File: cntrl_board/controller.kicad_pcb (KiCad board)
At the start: 2 copper layers, 223.5 x 91.7 mm, 419 parts, among them J1 PRG, J10 PRI_TRF_L, J11 PRI_TRF_N, J12 SEC_OUT_L, J13 SEC_OUT_N, J14 Left, J15 Right, J16 Conn_01x03_Male, J17 Conn_01x03_Male, J18 ch5, J19 ch6, J2 AMP_1, J20 ch1, J21 ch2, J22 ch3, J23 ch4, J24 AMP_4, J25 AMP_5, J26 AMP_6, J27 TP, J28 TP, J29 TP, J3 BUTTON, J30 TP, J31 TP, J32 TP, J33 TP, J34 TP, J35 TP, J36 TP, J37 TP, J38 TP, J39 TP, J4 AMP_2, J40 LCD, J41 TempSens1, J42 TempSens2, J43 TP, J44 TP, J45 TP, J46 TP, J47 USB, J48 PRG, J49 AFBR-2624Z, J5 AMP_3, J6 MAIN_PWR_L, J7 MAIN_PWR_N, J8 SEC_TRF_L, J9 SEC_TRF_N, M1 Fan_4pin, M2 Fan_4pin, Q1 STD2805, Q10 BC846A, Q11 BC846A, Q12 BC847, Q13 BC847, Q2 BC846A, Q3 BC847, Q4 BC847, Q5 BC847, Q6 BC847, Q7 BC847, Q8 BC847, Q9 BC847, U1 LM2596S-ADJ, U10 ADA4807-2ARM, U11 ADA4807-2ARM, U12 ADA4807-2ARM, U13 ADA4807-2ARM, U14 ADA4807-2ARM, U15 ADA4807-2ARM, U16 ADA4807-2ARM, U17 LM1085-ADJ, U18 LM1085-ADJ, U19 MCP130-xxxxTT, U2 ADAU1467WBCPZ300, U20 MCP130-xxxxTT, U21 24LC64, U3 25AA1024, U4 STM32F407VETx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

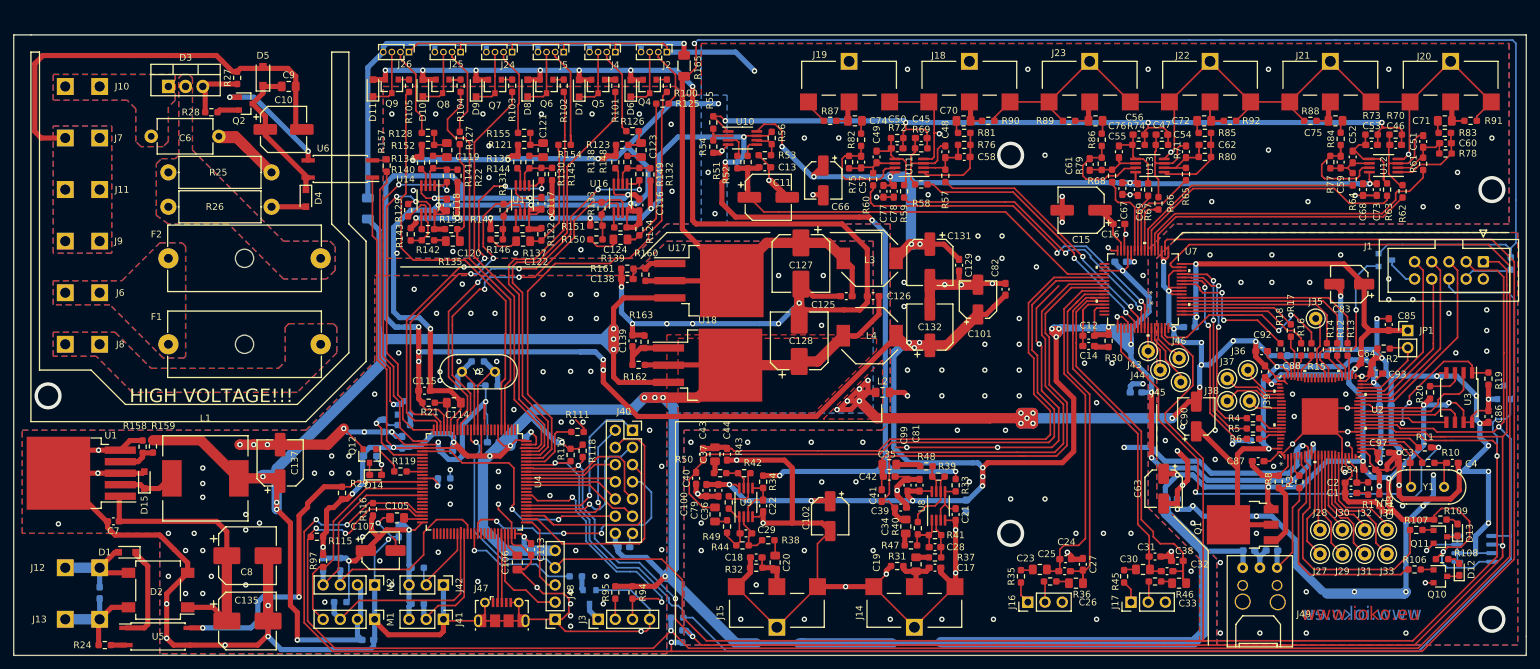
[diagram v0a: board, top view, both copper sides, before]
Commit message: update xformer soft startup
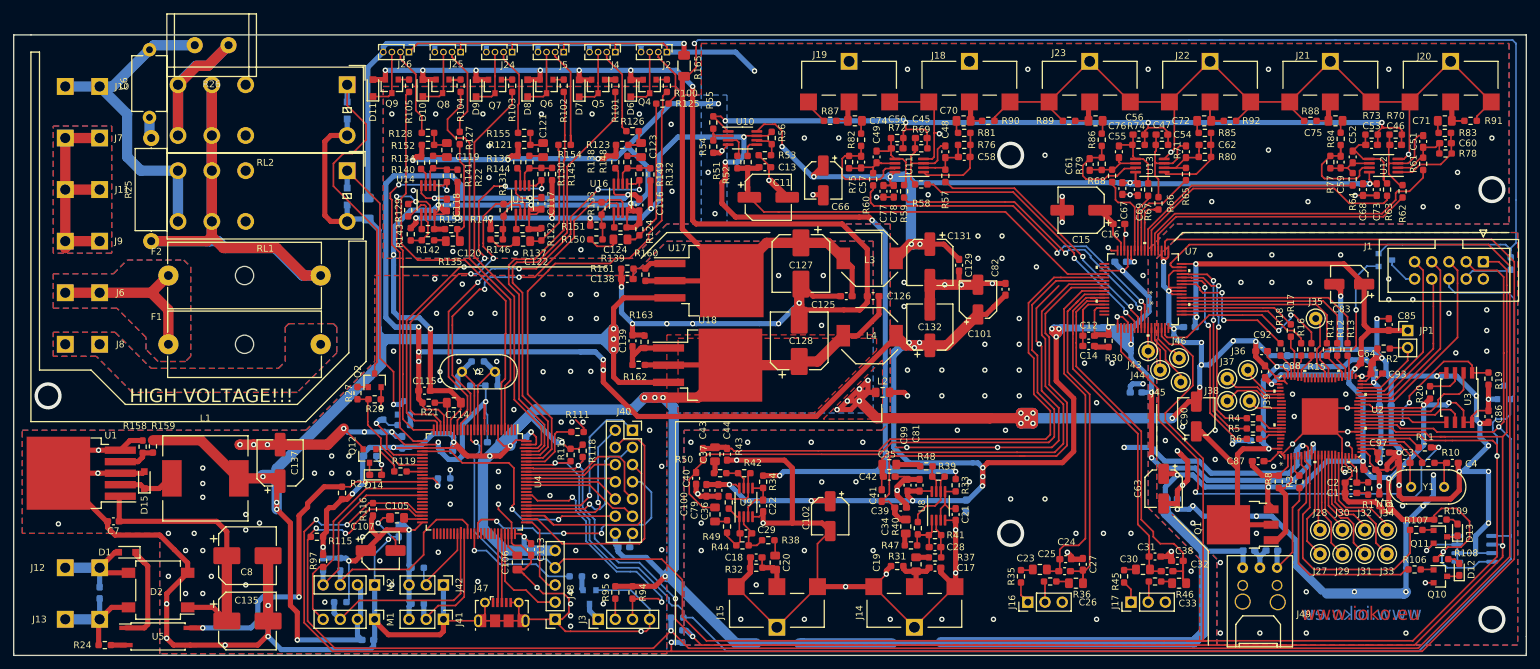
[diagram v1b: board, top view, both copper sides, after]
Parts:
- removed C10: 100uF, Capacitor_SMD:CP_Elec_6.3x7.7
- removed the C9 at (58.4, 50.8)
- removed D5: 12V, Diode_SMD:D_SOD-123F
- removed R157: 560, Resistor_SMD:R_0603_1608Metric_Pad0.98x0.95mm_HandSolder
- removed U6: SFH6186-4T, Package_SO:SO-4_7.6x3.6mm_P2.54mm
- added RL1: G2RL-2-DC12, Relay_THT:Relay_DPDT_Omron_G2RL, F.Cu at (67.1, 63.2)
- added RL2: G2RL-2-DC12, Relay_THT:Relay_DPDT_Omron_G2RL, F.Cu at (67.1, 50.5)
- C6: value 0.1uF/400V -> 0.01uF/630V
- D3: value MAC223A8X -> 1N4148; footprint Package_TO_SOT_THT:TO-220-3_Vertical -> Diode_SMD:D_SOD-323_HandSoldering; moved to B.Cu
- D4: moved to B.Cu
- Q2: value BC846A -> BC847
- R158: value 1K3 -> 2K
- R26: value 2K2/1W -> 47R/15W; footprint Resistor_THT:R_Axial_DIN0414_L11.9mm_D4.5mm_P15.24mm_Horizontal -> Resistor_THT:R_Radial_Power_L13.0mm_W9.0mm_P5.00mm
- R27: value 1K -> 10K
- R28: value 100 -> 10K
- R56: value 10K -> 1K
- moved R27 49.9 mm to (68.6, 96.1), turned to 270 degrees
- moved R28 48.8 mm to (71.1, 97.0)
- moved Q2 45.1 mm to (71.1, 94.2), turned to 90 degrees
- moved D3 31.0 mm to (67.1, 67.1), turned to 270 degrees
- moved R26 24.7 mm to (49.5, 44.7)
- moved D4 14.3 mm to (67.1, 54.4)
- moved C6 10.6 mm to (37.8, 55.4), turned to 90 degrees
- moved R25 10.5 mm to (38.1, 73.7), turned to 90 degrees
- moved F2 2.54 mm to (40.6, 78.7)
- renumbered C143 to C9
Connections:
- net Net-(C10-Pad1) renamed /ucu/AC_SS
- D3 pad 1: Net-(C6-Pad2) -> /ucu/AC_CTRL
- D3 pad 2: Net-(D3-Pad2) -> +12V
- D4 pad 2: Net-(D4-Pad2) -> +12V
- F2 pad 2: Net-(D3-Pad2) -> Net-(F2-Pad2)
- J1 pad 2: (no net) -> Net-(J1-Pad2)
- J11 pad 1: Net-(C10-Pad2) -> Net-(J11-Pad1)
- J47 pad 1: (no net) -> Net-(J47-Pad1)
- J47 pad 4: (no net) -> Net-(J47-Pad4)
- J49 pad 4: (no net) -> Net-(J49-Pad4)
- J49 pad 5: (no net) -> Net-(J49-Pad5)
- J7 pad 1: Net-(C10-Pad2) -> Net-(J11-Pad1)
- J9 pad 1: Net-(C10-Pad2) -> Net-(J11-Pad1)
- Q13 pad 3: Net-(Q13-Pad3) -> /ucu/AC_CTRL
- Q2 pad 2: Net-(Q2-Pad2) -> GND
- R25 pad 1: Net-(D3-Pad2) -> Net-(F2-Pad2)
- R26 pad 1: Net-(D4-Pad2) -> Net-(R26-Pad1)
- R26 pad 2: Net-(D3-Pad2) -> Net-(C6-Pad2)
- R27 pad 1: Net-(D3-Pad3) -> Net-(Q2-Pad1)
- R27 pad 2: Net-(C10-Pad2) -> Net-(R27-Pad2)
- R28 pad 1: Net-(Q2-Pad2) -> GND
- R28 pad 2: Net-(D3-Pad3) -> Net-(R27-Pad2)
- U2 pad 5: (no net) -> Net-(U2-Pad5)
- U2 pad 50: (no net) -> Net-(U2-Pad50)
- U2 pad 51: (no net) -> Net-(U2-Pad51)
- U2 pad 52: (no net) -> Net-(U2-Pad52)
- U2 pad 55: (no net) -> Net-(U2-Pad55)
- U2 pad 56: (no net) -> Net-(U2-Pad56)
- U2 pad 57: (no net) -> Net-(U2-Pad57)
- U2 pad 58: (no net) -> Net-(U2-Pad58)
- U2 pad 59: (no net) -> Net-(U2-Pad59)
- U2 pad 60: (no net) -> Net-(U2-Pad60)
- U2 pad 69: (no net) -> Net-(U2-Pad69)
- U2 pad 73: (no net) -> Net-(U2-Pad73)
- U2 pad 74: (no net) -> Net-(U2-Pad74)
- U2 pad 76: (no net) -> Net-(U2-Pad76)
- U2 pad 77: (no net) -> Net-(U2-Pad77)
- U2 pad 78: (no net) -> Net-(U2-Pad78)
- U2 pad 79: (no net) -> Net-(U2-Pad79)
- U2 pad 80: (no net) -> Net-(U2-Pad80)
- U2 pad 84: (no net) -> Net-(U2-Pad84)
- U2 pad 85: (no net) -> Net-(U2-Pad85)
- U2 pad 86: (no net) -> Net-(U2-Pad86)
- U4 pad 1: (no net) -> Net-(U4-Pad1)
- U4 pad 15: (no net) -> Net-(U4-Pad15)
- U4 pad 16: (no net) -> Net-(U4-Pad16)
- U4 pad 2: (no net) -> Net-(U4-Pad2)
- U4 pad 3: (no net) -> Net-(U4-Pad3)
- U4 pad 31: (no net) -> Net-(U4-Pad31)
- U4 pad 32: (no net) -> Net-(U4-Pad32)
- U4 pad 33: (no net) -> Net-(R27-Pad2)
- U4 pad 34: (no net) -> Net-(U4-Pad34)
- U4 pad 36: (no net) -> Net-(U4-Pad36)
- U4 pad 39: (no net) -> Net-(U4-Pad39)
- U4 pad 41: (no net) -> Net-(U4-Pad41)
- U4 pad 43: (no net) -> Net-(U4-Pad43)
- U4 pad 44: (no net) -> Net-(U4-Pad44)
- U4 pad 45: (no net) -> Net-(U4-Pad45)
- U4 pad 46: (no net) -> Net-(U4-Pad46)
- U4 pad 51: (no net) -> Net-(U4-Pad51)
- U4 pad 52: (no net) -> Net-(U4-Pad52)
- U4 pad 53: (no net) -> Net-(U4-Pad53)
- U4 pad 54: (no net) -> Net-(U4-Pad54)
- U4 pad 55: (no net) -> Net-(U4-Pad55)
- U4 pad 56: (no net) -> Net-(U4-Pad56)
- U4 pad 57: (no net) -> Net-(U4-Pad57)
- U4 pad 62: (no net) -> Net-(U4-Pad62)
- U4 pad 65: (no net) -> Net-(U4-Pad65)
- U4 pad 66: (no net) -> Net-(U4-Pad66)
- U4 pad 67: (no net) -> Net-(U4-Pad67)
- U4 pad 68: (no net) -> Net-(U4-Pad68)
- U4 pad 69: (no net) -> Net-(U4-Pad69)
- U4 pad 7: (no net) -> Net-(U4-Pad7)
- U4 pad 8: (no net) -> Net-(U4-Pad8)
- U4 pad 82: (no net) -> Net-(U4-Pad82)
- U4 pad 83: (no net) -> Net-(U4-Pad83)
- U4 pad 85: (no net) -> Net-(U4-Pad85)
- U4 pad 86: (no net) -> Net-(U4-Pad86)
- U4 pad 9: (no net) -> Net-(U4-Pad9)
- U7 pad 3: (no net) -> Net-(U7-Pad3)
- U7 pad 49: (no net) -> Net-(U7-Pad49)
- U7 pad 50: (no net) -> Net-(U7-Pad50)
- U7 pad 63: (no net) -> Net-(U7-Pad63)
- U7 pad 64: (no net) -> Net-(U7-Pad64)
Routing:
- net Net-(F2-Pad2): track 0.00 -> 100.5 mm
- net Net-(C10-Pad2): track 63.7 -> 0.00 mm
- net Net-(C6-Pad2): track 0.00 -> 49.6 mm
- net +3V3: track 792.5 -> 751.0 mm
- net /ucu/AC_CTRL: track 2.17 -> 41.7 mm, vias 0 -> 1
- net Net-(Q13-Pad3): track 37.4 -> 0.00 mm, vias 1 -> 0
- net Net-(R26-Pad1): track 0.00 -> 34.9 mm
- net Net-(J11-Pad1): track 0.00 -> 31.9 mm
- net /ucu/AC_SS: track 22.2 -> 52.0 mm
- net +12V: track 194.1 -> 220.5 mm
- net Net-(F1-Pad1): track 0.00 -> 25.0 mm
- net Net-(R27-Pad2): track 0.00 -> 17.5 mm
- net Net-(Q2-Pad1): track 17.6 -> 1.60 mm, vias 2 -> 0
- net Net-(C6-Pad1): track 14.7 -> 3.15 mm
- net Net-(D3-Pad3): track 9.19 -> 0.00 mm
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- added copper zone on B.Cu, net Net-(J11-Pad1)
- added copper zone on F.Cu, net Net-(J11-Pad1)
- removed copper zone on B.Cu, net Net-(C10-Pad2)
- removed copper zone on F.Cu, net Net-(C10-Pad2)
- removed copper zone on B.Cu, net Net-(C6-Pad2)
- removed copper zone on F.Cu, net Net-(C6-Pad2)
- removed copper zone on B.Cu, net Net-(D3-Pad2)
- removed copper zone on F.Cu, net Net-(D3-Pad2)

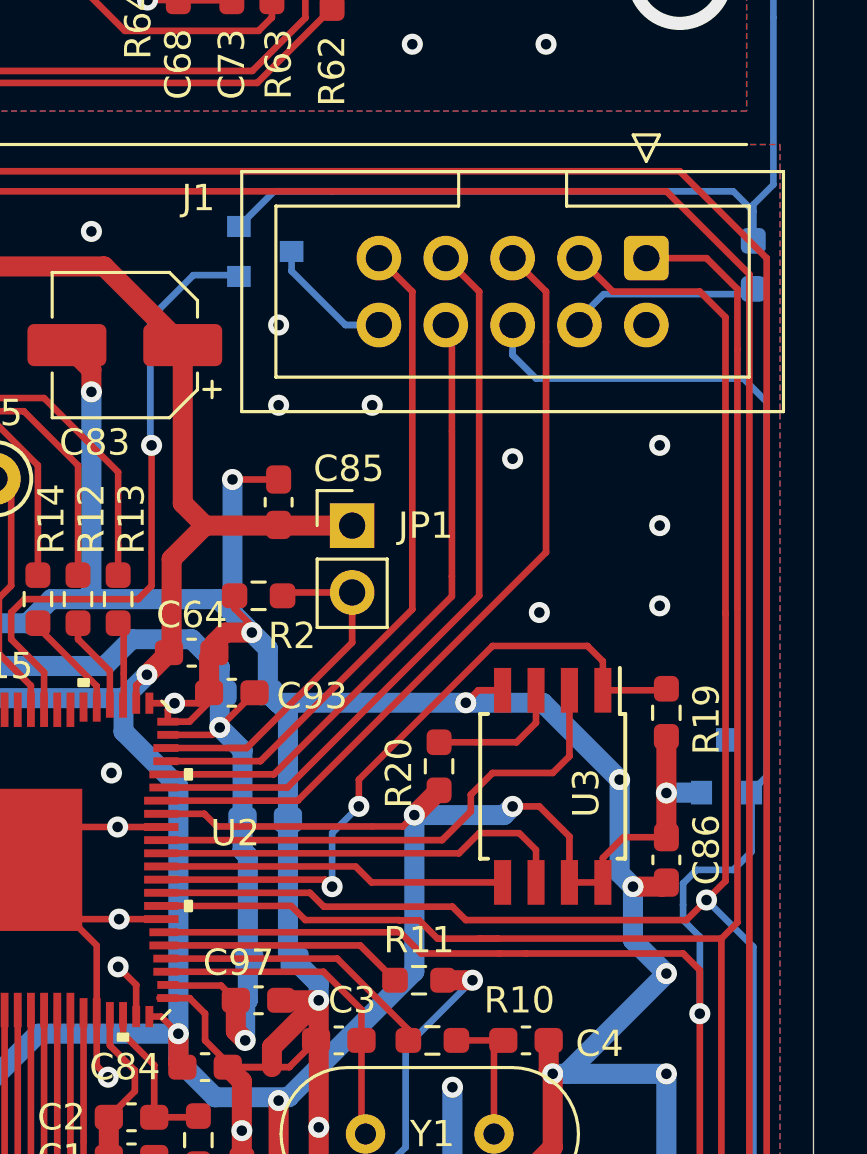
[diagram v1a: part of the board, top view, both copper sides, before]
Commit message: fix CPU-DSP channel
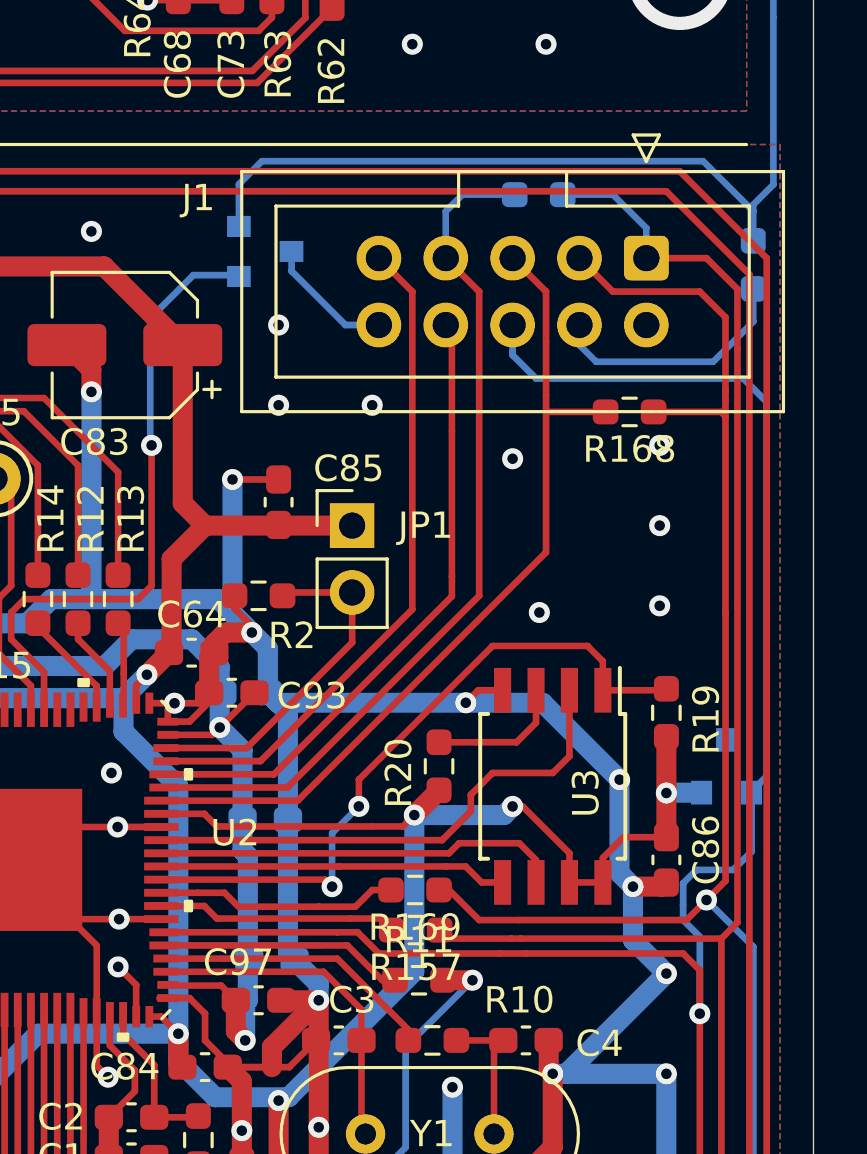
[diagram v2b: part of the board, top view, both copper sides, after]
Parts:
- added R157: DNP, Resistor_SMD:R_0603_1608Metric_Pad0.98x0.95mm_HandSolder, F.Cu at (226.2, 102.2)
- added R167: 0R, Resistor_SMD:R_0603_1608Metric_Pad0.98x0.95mm_HandSolder, B.Cu at (230.9, 74.3)
- added R168: 0R, Resistor_SMD:R_0603_1608Metric_Pad0.98x0.95mm_HandSolder, F.Cu at (234.3, 82.5)
- added R169: DNP, Resistor_SMD:R_0603_1608Metric_Pad0.98x0.95mm_HandSolder, F.Cu at (226.2, 100.7)
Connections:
- J1 pad 2: Net-(J1-Pad2) -> (no net)
- J47 pad 1: Net-(J47-Pad1) -> (no net)
- J47 pad 4: Net-(J47-Pad4) -> (no net)
- J49 pad 4: Net-(J49-Pad4) -> (no net)
- J49 pad 5: Net-(J49-Pad5) -> (no net)
- RL1 pad 2: Net-(RL1-Pad2) -> (no net)
- RL1 pad 7: Net-(RL1-Pad7) -> (no net)
- RL2 pad 2: Net-(RL2-Pad2) -> (no net)
- RL2 pad 7: Net-(RL2-Pad7) -> (no net)
- U2 pad 30: /ucu/DSP_SCL -> Net-(R157-Pad2)
- U2 pad 31: /ucu/DSP_SDA -> Net-(R169-Pad2)
- U2 pad 5: Net-(U2-Pad5) -> (no net)
- U2 pad 50: Net-(U2-Pad50) -> (no net)
- U2 pad 51: Net-(U2-Pad51) -> (no net)
- U2 pad 52: Net-(U2-Pad52) -> (no net)
- U2 pad 55: Net-(U2-Pad55) -> (no net)
- U2 pad 56: Net-(U2-Pad56) -> (no net)
- U2 pad 57: Net-(U2-Pad57) -> (no net)
- U2 pad 58: Net-(U2-Pad58) -> (no net)
- U2 pad 59: Net-(U2-Pad59) -> (no net)
- U2 pad 60: Net-(U2-Pad60) -> (no net)
- U2 pad 69: Net-(U2-Pad69) -> (no net)
- U2 pad 73: Net-(U2-Pad73) -> (no net)
- U2 pad 74: Net-(U2-Pad74) -> (no net)
- U2 pad 76: Net-(U2-Pad76) -> (no net)
- U2 pad 77: Net-(U2-Pad77) -> (no net)
- U2 pad 78: Net-(U2-Pad78) -> (no net)
- U2 pad 79: Net-(U2-Pad79) -> (no net)
- U2 pad 80: Net-(U2-Pad80) -> (no net)
- U2 pad 84: Net-(U2-Pad84) -> (no net)
- U2 pad 85: Net-(U2-Pad85) -> (no net)
- U2 pad 86: Net-(U2-Pad86) -> (no net)
- U4 pad 1: Net-(U4-Pad1) -> (no net)
- U4 pad 15: Net-(U4-Pad15) -> (no net)
- U4 pad 16: Net-(U4-Pad16) -> (no net)
- U4 pad 2: Net-(U4-Pad2) -> (no net)
- U4 pad 3: Net-(U4-Pad3) -> (no net)
- U4 pad 31: Net-(U4-Pad31) -> (no net)
- U4 pad 32: Net-(U4-Pad32) -> (no net)
- U4 pad 34: Net-(U4-Pad34) -> (no net)
- U4 pad 36: Net-(U4-Pad36) -> (no net)
- U4 pad 39: Net-(U4-Pad39) -> (no net)
- U4 pad 41: Net-(U4-Pad41) -> (no net)
- U4 pad 43: Net-(U4-Pad43) -> (no net)
- U4 pad 44: Net-(U4-Pad44) -> (no net)
- U4 pad 45: Net-(U4-Pad45) -> (no net)
- U4 pad 46: Net-(U4-Pad46) -> (no net)
- U4 pad 51: Net-(U4-Pad51) -> (no net)
- U4 pad 52: Net-(U4-Pad52) -> (no net)
- U4 pad 53: Net-(U4-Pad53) -> (no net)
- U4 pad 54: Net-(U4-Pad54) -> (no net)
- U4 pad 55: Net-(U4-Pad55) -> (no net)
- U4 pad 56: Net-(U4-Pad56) -> (no net)
- U4 pad 57: Net-(U4-Pad57) -> (no net)
- U4 pad 62: Net-(U4-Pad62) -> (no net)
- U4 pad 65: Net-(U4-Pad65) -> (no net)
- U4 pad 66: Net-(U4-Pad66) -> (no net)
- U4 pad 67: Net-(U4-Pad67) -> (no net)
- U4 pad 68: Net-(U4-Pad68) -> (no net)
- U4 pad 69: Net-(U4-Pad69) -> (no net)
- U4 pad 7: Net-(U4-Pad7) -> (no net)
- U4 pad 8: Net-(U4-Pad8) -> (no net)
- U4 pad 82: Net-(U4-Pad82) -> (no net)
- U4 pad 83: Net-(U4-Pad83) -> (no net)
- U4 pad 85: Net-(U4-Pad85) -> (no net)
- U4 pad 86: Net-(U4-Pad86) -> (no net)
- U4 pad 9: Net-(U4-Pad9) -> (no net)
- U7 pad 3: Net-(U7-Pad3) -> (no net)
- U7 pad 49: Net-(U7-Pad49) -> (no net)
- U7 pad 50: Net-(U7-Pad50) -> (no net)
- U7 pad 63: Net-(U7-Pad63) -> (no net)
- U7 pad 64: Net-(U7-Pad64) -> (no net)
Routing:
- net Net-(R169-Pad2): track 0.00 -> 9.21 mm
- net Net-(R157-Pad2): track 0.00 -> 9.13 mm
- net /ucu/DSP_SDA: track 244.3 -> 236.6 mm
- net /ucu/DSP_SCL: track 242.0 -> 235.1 mm
- net /dsp/SCLK_M: track 28.3 -> 33.0 mm
- net /dsp/MISO_M: track 30.2 -> 32.5 mm
- net Net-(J1-Pad4): track 7.32 -> 9.51 mm
- net +5V: track 252.6 -> 254.5 mm
- net /dsp/SB_SCK: track 16.1 -> 15.5 mm
